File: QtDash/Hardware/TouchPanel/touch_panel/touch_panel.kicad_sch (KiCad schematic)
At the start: 11 parts, among them U1 74LVC2G14, U2 74LVC2G14, U3 AT42QT1070-S

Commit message: bugfix/hardware-revc-fixes: 	- first draft of layout for control button board 	- added symbol + footprint for capacitive touch button 12.5mm square
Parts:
- added J1: Conn_01x06_Male, Connector_JST:JST_GH_SM06B-GHS-TB_1x06-1MP_P1.25mm_Horizontal, symbol Connector:Conn_01x06_Male
- added SW1, SW2, SW3, SW4: CapTouch_pad, volvodash:CAPTOUCH_12.5, symbol volvodash:CapTouch_pad
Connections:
- net GND: now also J1.1 (Pin_1), SW1.2, SW2.2, SW3.2, SW4.2
- net VCC: now also J1.6 (Pin_6)
- net at R4.2: now also SW3.1
- net USER_INPUT2: now reaches U2.4
- net USER_INPUT2: now also J1.4 (Pin_4)
- net at R5.2: now also SW4.1
- net USER_INPUT3: now reaches U1.6
- net USER_INPUT3: now also J1.3 (Pin_3)
- net at R2.2: now also SW1.1
- net USER_INPUT1: now reaches U2.6
- net USER_INPUT1: now also J1.5 (Pin_5)
- net at R3.2: now also SW2.1
- net USER_INPUT4: now reaches U1.4
- net USER_INPUT4: now also J1.2 (Pin_2)
- net GUARD_LOOP: now reaches R1.2

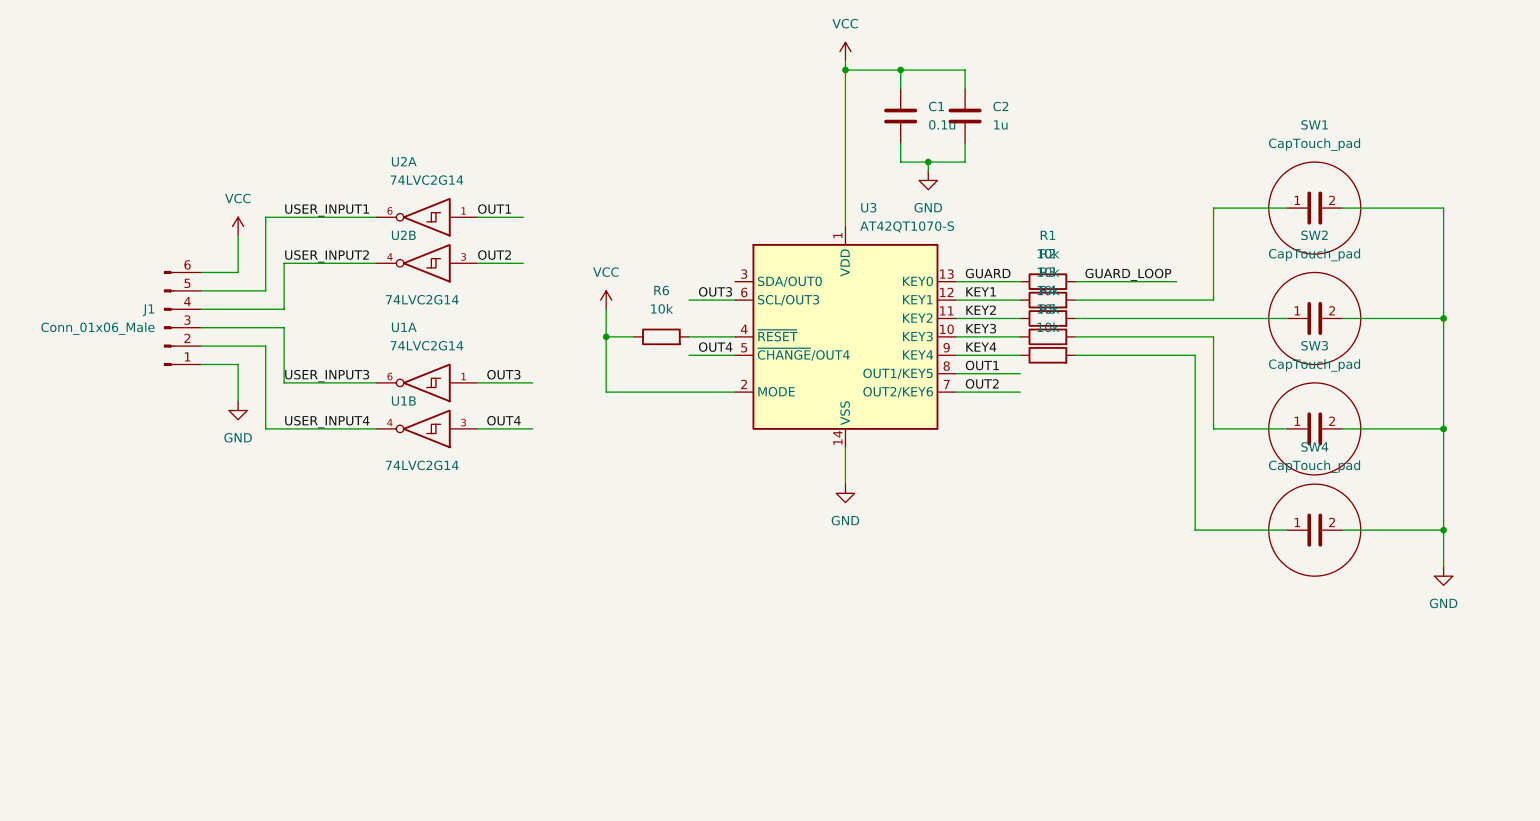
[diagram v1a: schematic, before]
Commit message: bugfix/hardware-revc-fixes: 	- finalized touch panel rev A 	- Rev A touch panel board sent to fab 	- added stl files for small guage slot cover (whole and cutout for touch panel board)
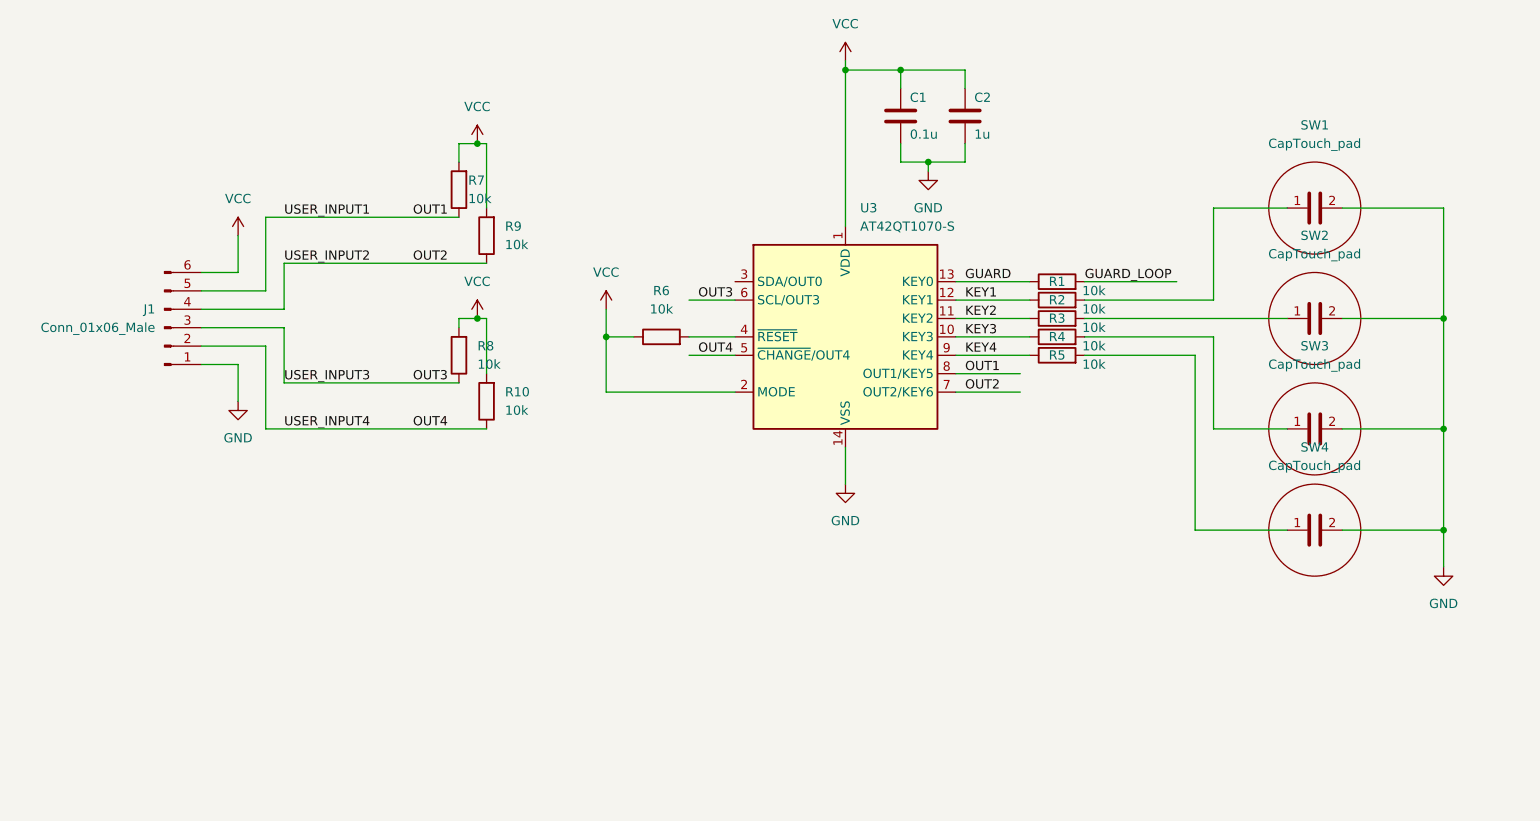
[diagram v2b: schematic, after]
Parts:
- removed U1, U2: 74LVC2G14, Package_SO:TSOP-6_1.65x3.05mm_P0.95mm, symbol 74xGxx:74LVC2G14
- added R10, R7, R8, R9: 10k, Resistor_SMD:R_0603_1608Metric_Pad0.98x0.95mm_HandSolder, symbol Device:R
- J1: footprint Connector_JST:JST_GH_SM06B-GHS-TB_1x06-1MP_P1.25mm_Horizontal -> Connector_JST:JST_PH_S6B-PH-SM4-TB_1x06-1MP_P2.00mm_Horizontal
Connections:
- net USER_INPUT1 is gone; now on net OUT1: J1.5 (Pin_5)
- net USER_INPUT2 is gone; now on net OUT2: J1.4 (Pin_4)
- net USER_INPUT3 is gone; now on net OUT3: J1.3 (Pin_3)
- net USER_INPUT4 is gone; now on net OUT4: J1.2 (Pin_2)
- net OUT1: now also R7.1
- net OUT2: now also R9.1
- net OUT3: now also R8.1
- net OUT4: now also R10.1
- net VCC: now also R10.2, R7.2, R8.2, R9.2
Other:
- moved on the sheet: R1, R2, R3, R4, R5

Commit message: bugfix/hardware-revc-fixes: 	- added documentation for rev A touch panel board
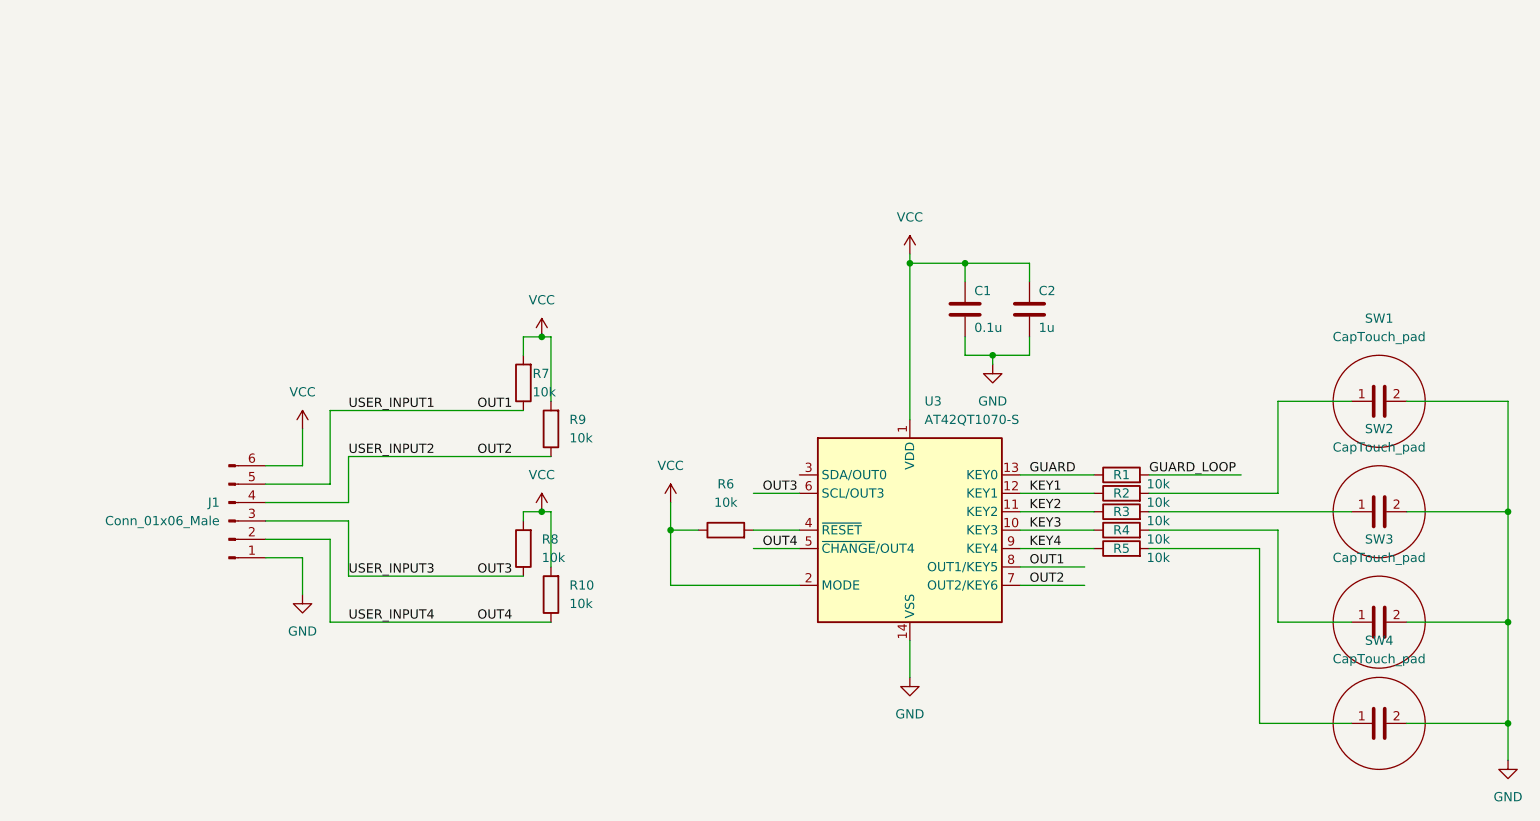
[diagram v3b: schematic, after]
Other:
- title: (none) -> Volvo 240 Digital Digital Dash Control Panel CapTouch
- moved on the sheet: C1, C2, J1, R1, R10, R2, R3, R4, R5, R6, R7, R8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
